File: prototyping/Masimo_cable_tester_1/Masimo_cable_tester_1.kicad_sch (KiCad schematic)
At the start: 28 parts, among them J1 Touchscreen HMI, J10 5V Jumper, J16 Debug Connections, J17 Banana Jack, J2 Conn_01x28_Socket, J3 Conn_01x28_Socket, J4 Barrel Jack 9V, J5 Conn_01x08, J6 SFML-110-02-L-D-A, J7 Conn_01x03_Pin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

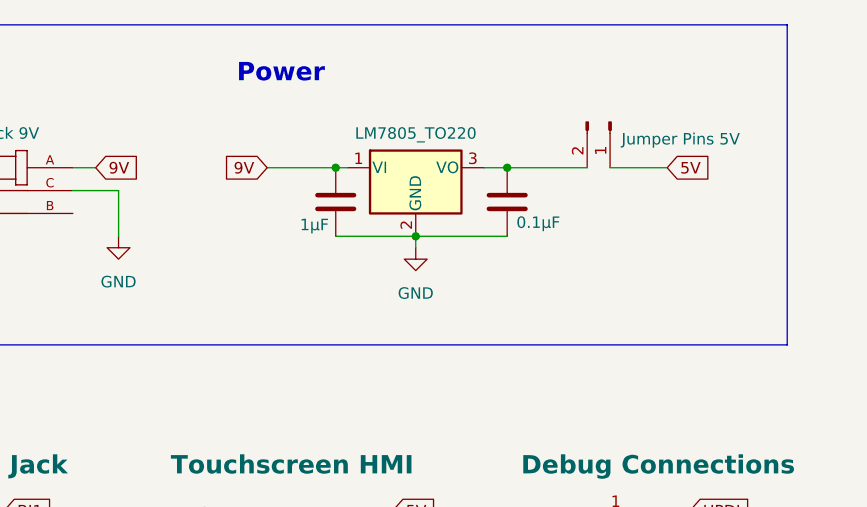
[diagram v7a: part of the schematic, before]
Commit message: Prototype PCB updates and additions
Consolidated the KiCad symbols and footprints used into a single folder to be used. Updated jumper footprints and started to organize the PCB components. (no traces yet).
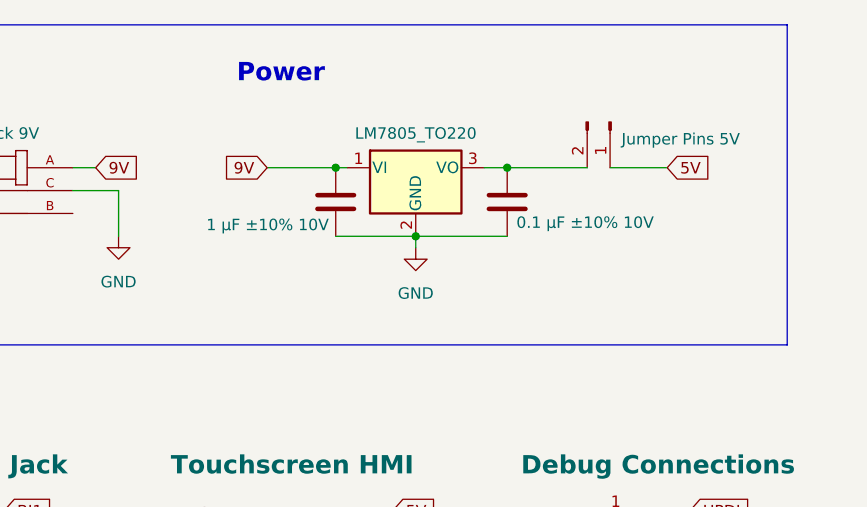
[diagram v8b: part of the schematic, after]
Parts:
- C1: value 1µF -> 1 µF ±10% 10V; footprint CL10B105KP8NNNC:CAP_CL10_SAM -> KiCad Symbols and Footprints:CAP_CL10_SAM
- C2: value 0.1µF -> 0.1 µF ±10% 10V; footprint CL05B104KP5NNNC:CAP_CL05_SAM -> KiCad Symbols and Footprints:CAP_CL05_SAM
- J10, J8, J9: footprint (none) -> Connector_PinHeader_2.54mm:PinHeader_1x02_P2.54mm_Vertical
- J4: footprint 54_00129:TENSILITY_54-00129 -> KiCad Symbols and Footprints:TENSILITY_54-00129
- J6: footprint SFML_110_02_L_D_A:SAMTEC_SFML-110-02-L-D-A -> KiCad Symbols and Footprints:SAMTEC_SFML-110-02-L-D-A
- R1: footprint ERJ_2RKF1002X:RC0402N_PAN -> KiCad Symbols and Footprints:RC0402N_PAN
- R10, R11, R12, R3, R4, R5, R6, R7, R8, R9: footprint RG1608P-102-B-T5:RES_0816_SUS -> KiCad Symbols and Footprints:RES_0816_SUS
- U1: footprint J104D2C5VDC.20S:RELAY8_J104D2C5VDC.20S_CRS -> KiCad Symbols and Footprints:RELAY8_J104D2C5VDC.20S_CRS
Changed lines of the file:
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@@
 			)
 		)
-		(property "Footprint" "RG1608P-102-B-T5:RES_0816_SUS"
+		(property "Footprint" "KiCad Symbols and Footprints:RES_0816_SUS"
 			(at 222.25 71.628 90)
 			(effects
@@
 			)
 		)
-		(property "Footprint" "RG1608P-102-B-T5:RES_0816_SUS"
+		(property "Footprint" "KiCad Symbols and Footprints:RES_0816_SUS"
 			(at 222.25 91.948 90)
 			(effects
@@
 			)
 		)
-		(property "Footprint" "RG1608P-102-B-T5:RES_0816_SUS"
+		(property "Footprint" "KiCad Symbols and Footprints:RES_0816_SUS"
 			(at 222.25 131.318 90)
 			(effects
@@
 			)
 		)
-		(property "Value" "0.1µF"
+		(property "Value" "0.1 µF ±10% 10V"
 			(at 91.186 46.736 0)
 			(effects
@@
 			)
 		)
-		(property "Footprint" "CL05B104KP5NNNC:CAP_CL05_SAM"
+		(property "Footprint" "KiCad Symbols and Footprints:CAP_CL05_SAM"
 			(at 91.1352 48.26 0)
 			(effects
@@
 			)
 		)
-		(property "Footprint" "RG1608P-102-B-T5:RES_0816_SUS"
+		(property "Footprint" "KiCad Symbols and Footprints:RES_0816_SUS"
 			(at 222.25 102.108 90)
 			(effects
@@
 			)
 		)
-		(property "Footprint" ""
+		(property "Footprint" "Connector_PinHeader_2.54mm:PinHeader_1x02_P2.54mm_Vertical"
 			(at 101.6 35.56 0)
 			(effects
@@
 			)
 		)
-		(property "Footprint" "RG1608P-102-B-T5:RES_0816_SUS"
+		(property "Footprint" "KiCad Symbols and Footprints:RES_0816_SUS"
 			(at 222.25 141.478 90)
 			(effects
@@
 			)
 		)
-		(property "Footprint" "RG1608P-102-B-T5:RES_0816_SUS"
+		(property "Footprint" "KiCad Symbols and Footprints:RES_0816_SUS"
 			(at 222.25 110.998 90)
 			(effects
@@
 			)
 		)
-		(property "Footprint" "SFML_110_02_L_D_A:SAMTEC_SFML-110-02-L-D-A"
+		(property "Footprint" "KiCad Symbols and Footprints:SAMTEC_SFML-110-02-L-D-A"
 			(at 153.67 92.71 0)
 			(effects
@@
 			)
 		)
-		(property "Footprint" "ERJ_2RKF1002X:RC0402N_PAN"
+		(property "Footprint" "KiCad Symbols and Footprints:RC0402N_PAN"
 			(at 160.782 31.75 90)
 			(effects
@@
 			)
 		)
-		(property "Value" "1µF"
+		(property "Value" "1 µF ±10% 10V"
 			(at 70.358 46.99 0)
 			(effects
@@
 			)
 		)
-		(property "Footprint" "CL10B105KP8NNNC:CAP_CL10_SAM"
+		(property "Footprint" "KiCad Symbols and Footprints:CAP_CL10_SAM"
 			(at 70.1548 48.26 0)
 			(effects
@@
 			)
 		)
-		(property "Footprint" "54_00129:TENSILITY_54-00129"
+		(property "Footprint" "KiCad Symbols and Footprints:TENSILITY_54-00129"
 			(at 36.83 43.18 0)
 			(effects
@@
 			)
 		)
-		(property "Footprint" "RG1608P-102-B-T5:RES_0816_SUS"
+		(property "Footprint" "KiCad Symbols and Footprints:RES_0816_SUS"
 			(at 222.25 62.738 90)
 			(effects
@@
 			)
 		)
-		(property "Footprint" "RG1608P-102-B-T5:RES_0816_SUS"
+		(property "Footprint" "KiCad Symbols and Footprints:RES_0816_SUS"
 			(at 222.25 121.158 90)
 			(effects
@@
 			)
 		)
-		(property "Footprint" "J104D2C5VDC.20S:RELAY8_J104D2C5VDC.20S_CRS"
+		(property "Footprint" "KiCad Symbols and Footprints:RELAY8_J104D2C5VDC.20S_CRS"
 			(at 125.73 143.51 0)
 			(effects
@@
 			)
 		)
-		(property "Footprint" ""
+		(property "Footprint" "Connector_PinHeader_2.54mm:PinHeader_1x02_P2.54mm_Vertical"
 			(at 90.17 115.57 0)
 			(effects
@@
 			)
 		)
-		(property "Footprint" "RG1608P-102-B-T5:RES_0816_SUS"
+		(property "Footprint" "KiCad Symbols and Footprints:RES_0816_SUS"
 			(at 222.25 151.638 90)
 			(effects
@@
 			)
 		)
-		(property "Footprint" "RG1608P-102-B-T5:RES_0816_SUS"
+		(property "Footprint" "KiCad Symbols and Footprints:RES_0816_SUS"
 			(at 222.25 81.788 90)
 			(effects
@@
 			)
 		)
-		(property "Footprint" ""
+		(property "Footprint" "Connector_PinHeader_2.54mm:PinHeader_1x02_P2.54mm_Vertical"
 			(at 87.63 135.89 0)
 			(effects
